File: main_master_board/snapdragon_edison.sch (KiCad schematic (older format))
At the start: 49 parts, among them J2 J0C-0005NLT, U17 J1, U18 J2, U19 LAN9512, U21 MIC2026, U24 AS1360, U25 Si1900DL, U26 SN74LV4T125, U27 SN74LV4T125, U28 SN74LV1T125, Y1 SG-310SCCN 25.000MJ3

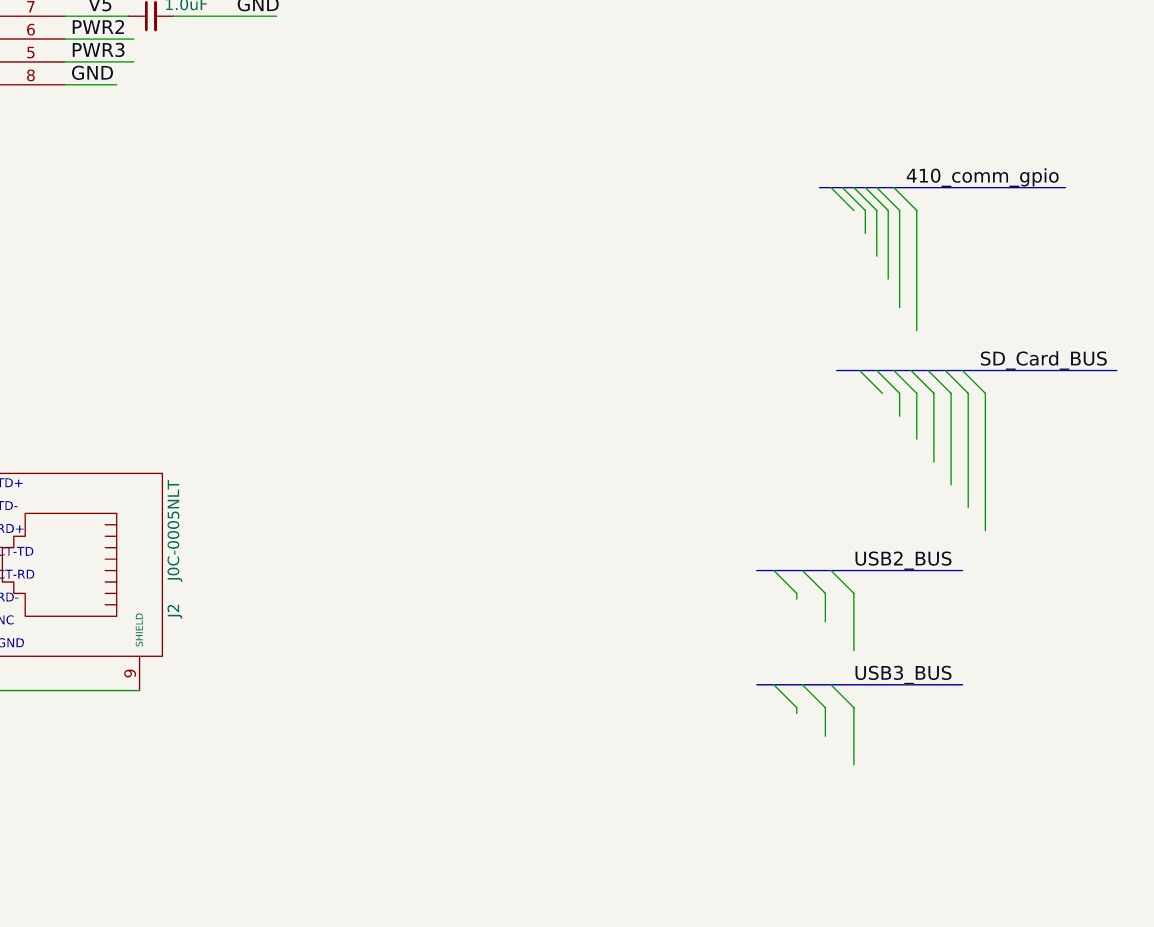
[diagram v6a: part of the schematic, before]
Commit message: Updated the RJ45 to through hole. Moved connectors about
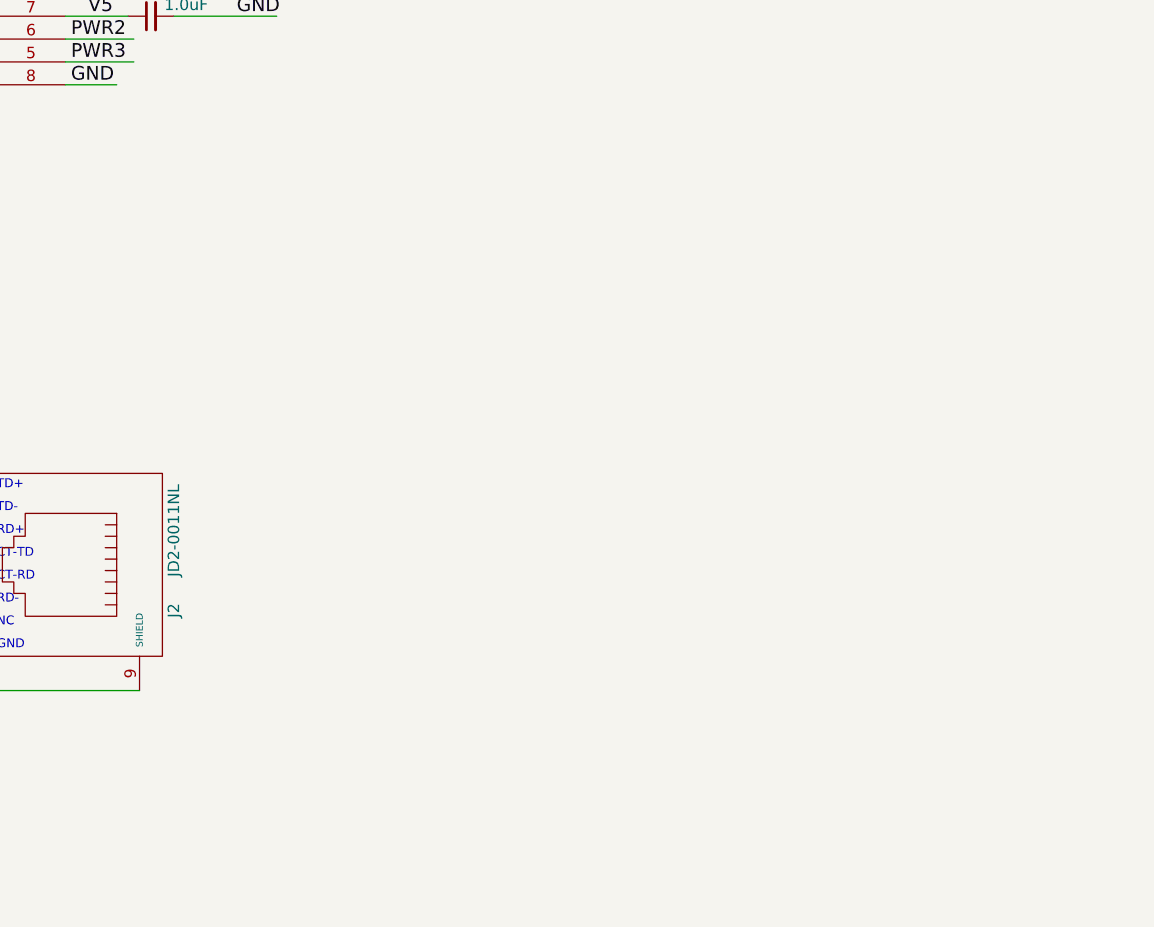
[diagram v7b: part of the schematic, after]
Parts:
- J2: value J0C-0005NLT -> JD2-0011NL; footprint Pulse_Electronics:J0C -> Pulse_Electronics:JD2-0011NL
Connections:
- net labels removed: 410_comm_gpio, SD_Card_BUS, USB2_BUS, USB3_BUS
- wire segments 396 -> 379
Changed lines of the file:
@@
 LIBS:Sensors
 LIBS:LP3852-3.3
-LIBS:decaWave
+LIBS:0s102011ma1qn1
+LIBS:74LVC1G17
+LIBS:74V1T126
+LIBS:acs711klctr-12ab-t
+LIBS:AD7192
+LIBS:AD7193
+LIBS:am-hrr30-xxx
+LIBS:aon7528
+LIBS:AP7363
+LIBS:AS1359
+LIBS:csd16323q3
+LIBS:dmn2004dmk
+LIBS:dp_devices
+LIBS:DSPIC33E128MC506
+LIBS:fds6898az
+LIBS:ina197
+LIBS:irf7329pbf
+LIBS:ld1117
+LIBS:lm3478
+LIBS:lm3481
+LIBS:lt1910
+LIBS:ltc1871
+LIBS:ltc1982
+LIBS:MAG3110
+LIBS:mcp1700
+LIBS:mcp73831
+LIBS:mcsmt-g5030a1-3712
+LIBS:microchip_can
+LIBS:microclasp_hdrx2
+LIBS:microclasp_hdrx3
+LIBS:MPU-6000_MPU-6050
+LIBS:MPU-9150
+LIBS:nrf24l01+
+LIBS:pds1040l
+LIBS:pic12f1571
+LIBS:pinhead
+LIBS:psmn013-80ys
+LIBS:RESISTOR_ARRAY
+LIBS:rf803d
+LIBS:RGB_LED
+LIBS:Si1970DH
+LIBS:sn65hvd232
+LIBS:ssc54
+LIBS:sw_push_4
+LIBS:tc74
+LIBS:TPS2113A
+LIBS:tps54540
+LIBS:vs-mbrb1635pbf
+LIBS:xal5050-562meb
+LIBS:xal6030-182mec
 LIBS:conn_2x50
 LIBS:conn_open_q_x2
@@
 LIBS:ac-dc
 LIBS:actel
-LIBS:allegro
 LIBS:Altera
 LIBS:analog_devices
@@
 LIBS:logo
 LIBS:maxim
-LIBS:mechanical
 LIBS:microchip_dspic33dsc
 LIBS:microchip_pic10mcu
@@
 LIBS:microchip_pic32mcu
 LIBS:motor_drivers
-LIBS:motors
 LIBS:msp430
 LIBS:nordicsemi
@@
 LIBS:ttl_ieee
 LIBS:video
-LIBS:wiznet
 LIBS:Worldsemi
 LIBS:Xicor
-LIBS:zetex
 LIBS:Zilog
 LIBS:conn_2x45
@@
 P 11300 8900
 F 0 "J2" H 11500 9400 50  0000 C CNN
-F 1 "J0C-0005NLT" H 11150 9400 50  0000 C CNN
-F 2 "Pulse_Electronics:J0C" H 11300 8900 50  0001 C CNN
-F 3 "http://www.digikey.com/product-detail/en/J0C-0005NLT/553-2067-1-ND/3687443?curr=usd&WT.z_cid=ref_octopart_dkc_buynow&site=us" H 11300 8900 50  0001 C CNN
+F 1 "JD2-0011NL" H 11150 9400 50  0000 C CNN
+F 2 "Pulse_Electronics:JD2-0011NL" H 11300 8900 50  0001 C CNN
+F 3 "http://www.digikey.com/product-detail/en/JD2-0011NL/553-2609-ND/5305032?curr=usd&WT.z_cid=ref_octopart_dkc_buynow&site=usdetail/en/J0C-0005NLT/553-2067-1-ND/3687443?curr=usd&WT.z_cid=ref_octopart_dkc_buynow&site=us" H 11300 8900 50  0001 C CNN
 	1    11300 8900
 	0    1    1    0
@@
 Wire Wire Line
 	1600 3000 2050 3000
-Wire Bus Line
-	14350 8925 15250 8925
-Entry Wire Line
-	14425 8925 14525 9025
-Entry Wire Line
-	14550 8925 14650 9025
-Entry Wire Line
-	14675 8925 14775 9025
 Text Label 14675 3950 2    60   ~ 0
 PRTCTL2
-Wire Wire Line
-	14525 9025 14525 9050
 Text Label 14675 4050 2    60   ~ 0
 USBDP2
 Text Label 14675 4150 2    60   ~ 0
 USBDM2
-Wire Wire Line
-	14650 9025 14650 9150
-Wire Wire Line
-	14775 9025 14775 9275
-Text Label 14775 8925 0    60   ~ 0
-USB2_BUS
-Wire Bus Line
-	14350 9425 15250 9425
-Entry Wire Line
-	14425 9425 14525 9525
-Entry Wire Line
-	14550 9425 14650 9525
-Entry Wire Line
-	14675 9425 14775 9525
 Text Label 14675 4325 2    60   ~ 0
 PRTCTL3
-Wire Wire Line
-	14525 9525 14525 9550
 Text Label 14675 4425 2    60   ~ 0
 USBDP3
 Text Label 14675 4525 2    60   ~ 0
 USBDM3
-Wire Wire Line
-	14650 9525 14650 9650
-Wire Wire Line
-	14775 9525 14775 9775
-Text Label 14775 9425 0    60   ~ 0
-USB3_BUS
-Wire Bus Line
-	14700 8050 15925 8050
-Entry Wire Line
-	14800 8050 14900 8150
-Entry Wire Line
-	14875 8050 14975 8150
-Entry Wire Line
-	14950 8050 15050 8150
-Entry Wire Line
-	15025 8050 15125 8150
-Entry Wire Line
-	15100 8050 15200 8150
-Entry Wire Line
-	15175 8050 15275 8150
-Entry Wire Line
-	15250 8050 15350 8150
-Wire Wire Line
-	14975 8250 14975 8150
-Wire Wire Line
-	15050 8350 15050 8150
-Wire Wire Line
-	15125 8450 15125 8150
-Wire Wire Line
-	15200 8550 15200 8150
-Wire Wire Line
-	15275 8650 15275 8150
-Wire Wire Line
-	15350 8750 15350 8150
-Text Label 15325 8050 0    60   ~ 0
-SD_Card_BUS
 Text Label 14675 2875 2    60   ~ 0
 I2C1_SCL
@@
 Text Label 14675 2775 2    60   ~ 0
 UART0_CTS_N
-Wire Bus Line
-	14625 7250 15700 7250
-Text Label 15675 7250 2    60   ~ 0
-410_comm_gpio
-Entry Wire Line
-	14675 7250 14775 7350
-Entry Wire Line
-	14725 7250 14825 7350
-Entry Wire Line
-	14775 7250 14875 7350
-Entry Wire Line
-	14825 7250 14925 7350
-Entry Wire Line
-	14875 7250 14975 7350
-Entry Wire Line
-	14950 7250 15050 7350
-Wire Wire Line
-	14825 7450 14825 7350
-Wire Wire Line
-	14875 7550 14875 7350
-Wire Wire Line
-	14925 7650 14925 7350
-Wire Wire Line
-	14975 7775 14975 7350
-Wire Wire Line
-	15050 7875 15050 7350
 Text HLabel 14700 2350 2    60   Output ~ 0
 1V8
